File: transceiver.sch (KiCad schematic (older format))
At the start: 44 parts, among them U3 CC1200, Y1 Crystal_GND24

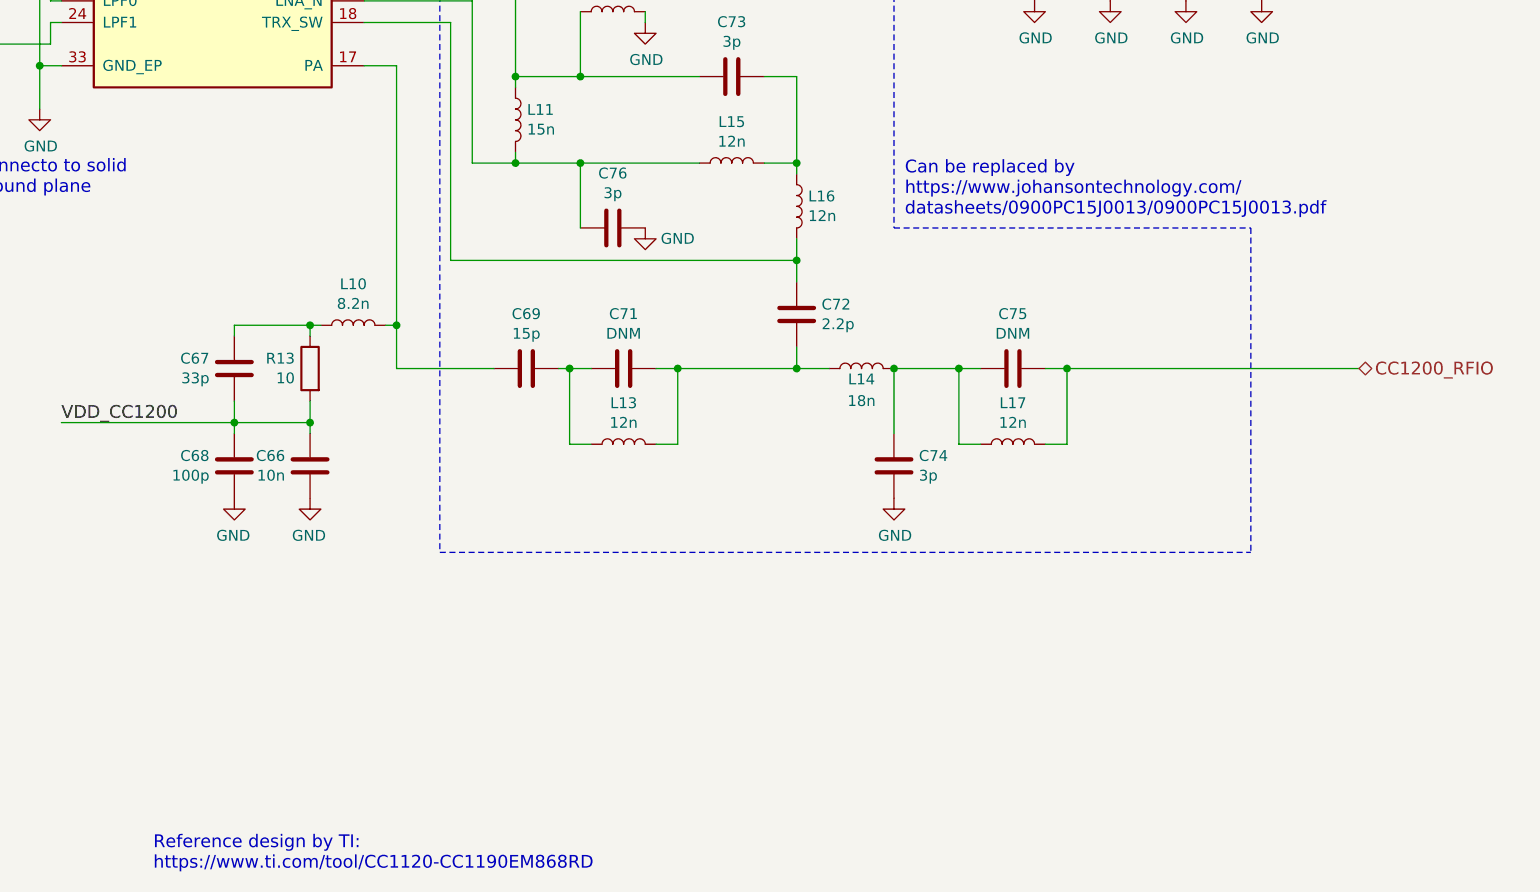
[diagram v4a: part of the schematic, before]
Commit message: Added mounting holes and terminal block
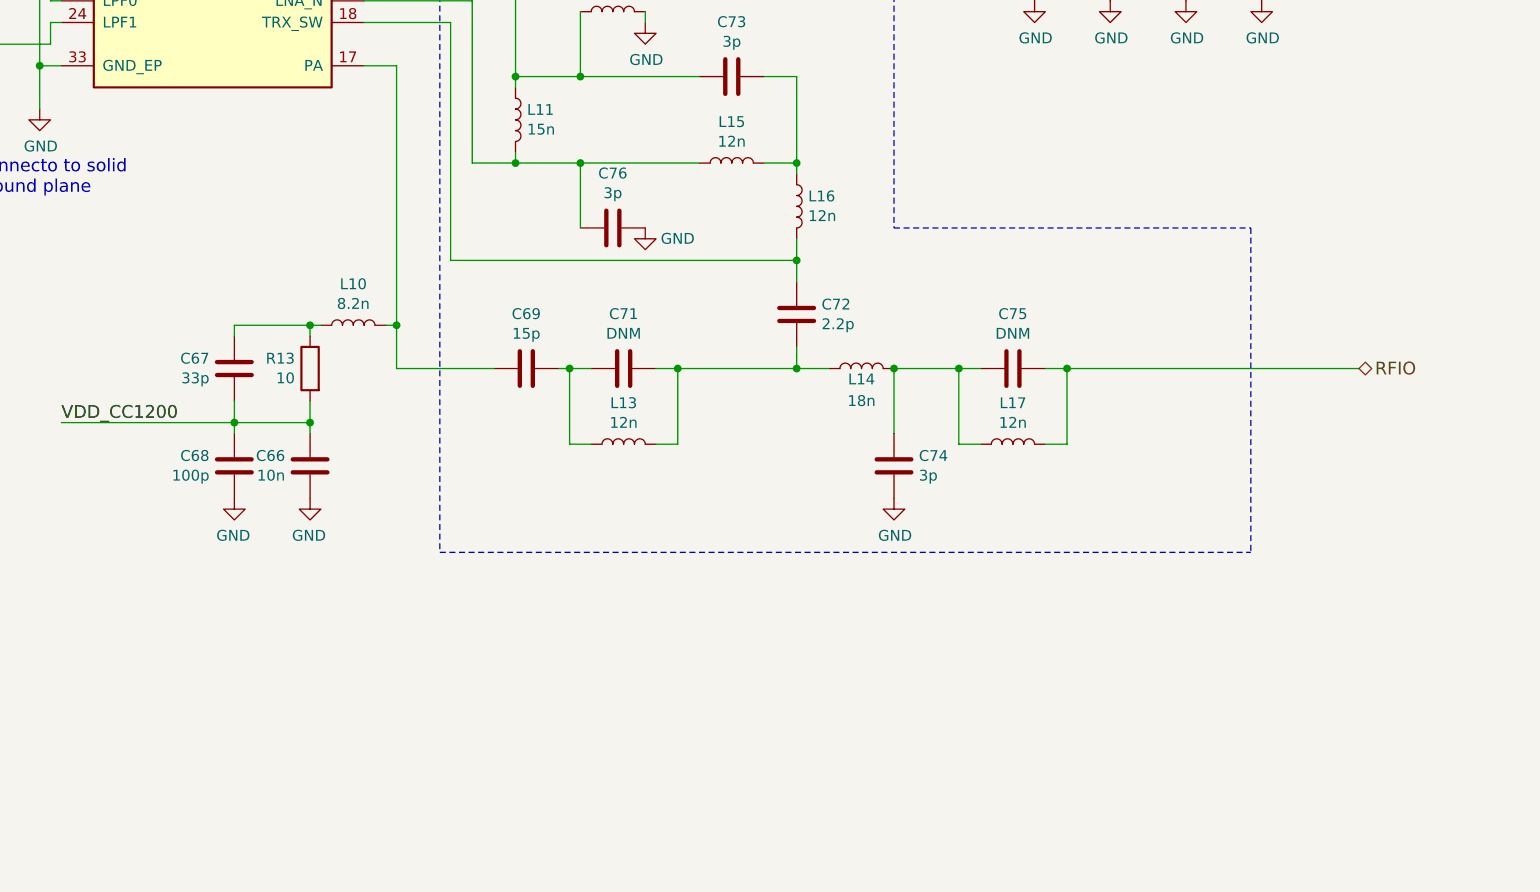
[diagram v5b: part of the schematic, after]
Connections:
- net CC1200_RFIO renamed RFIO
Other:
- note removed: "Can be replaced by \nhttps://www.johansontechnology.com/\ndatasheets/0900PC15J0013/0900PC15J0013.pdf"
- note removed: "Reference design by TI:\nhttps://www.ti.com/tool/CC1120-CC1190EM868RD\n"
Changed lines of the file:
@@
 	8650 5300 10000 5300
 Text HLabel 10000 5300 2    59   BiDi ~ 0
-CC1200_RFIO
+RFIO
 Connection ~ 7850 5300
 Wire Wire Line
@@
 Wire Notes Line
 	7850 4650 9500 4650
-Text Notes 7900 4600 0    59   ~ 0
-Can be replaced by \nhttps://www.johansontechnology.com/\ndatasheets/0900PC15J0013/0900PC15J0013.pdf
 Wire Wire Line
 	6700 3650 6700 3700
@@
 Wire Wire Line
 	3350 2900 3350 3000
-Text Notes 4425 7625 0    59   ~ 0
-Reference design by TI:\nhttps://www.ti.com/tool/CC1120-CC1190EM868RD\n
 Text Notes 1025 2600 0    59   ~ 0
 Can also use temperature compensated crystal.\nBut probably not neccecairy.

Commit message: Routed power for RF
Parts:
- removed TP2: VDD_CC1200, TestPoint:TestPoint_Pad_2.0x2.0mm, symbol Connector:TestPoint
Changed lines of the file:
@@
 $Descr A4 11693 8268
 encoding utf-8
-Sheet 4 6
+Sheet 3 6
 Title ""
 Date ""
@@
 	3750 1150 5400 1150
 Connection ~ 3750 1150
-Connection ~ 5400 1150
 Wire Wire Line
 	5400 1150 5400 1900
 Wire Wire Line
-	5675 1150 5400 1150
-$Comp
-L Connector:TestPoint TP2
-U 1 1 603797AA
-P 5675 1150
-F 0 "TP2" V 5629 1338 50  0000 L CNN
-F 1 "VDD_CC1200" V 5720 1338 50  0000 L CNN
-F 2 "TestPoint:TestPoint_Pad_2.0x2.0mm" H 5875 1150 50  0001 C CNN
-F 3 "~" H 5875 1150 50  0001 C CNN
-	1    5675 1150
-	0    1    1    0
-$EndComp
-Wire Wire Line
 	5900 4350 6100 4350

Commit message: Fixed (most) pwr flag issues
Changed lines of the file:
@@
 	0    -1   -1   0
 $EndComp
+$Comp
+L power:PWR_FLAG #FLG0102
+U 1 1 602E2A41
+P 5400 1050
+F 0 "#FLG0102" H 5400 1125 50  0001 C CNN
+F 1 "PWR_FLAG" H 5400 1223 50  0000 C CNN
+F 2 "" H 5400 1050 50  0001 C CNN
+F 3 "~" H 5400 1050 50  0001 C CNN
+	1    5400 1050
+	1    0    0    -1
+$EndComp
+Wire Wire Line
+	5400 1050 5400 1150
+Connection ~ 5400 1150
 $EndSCHEMATC
